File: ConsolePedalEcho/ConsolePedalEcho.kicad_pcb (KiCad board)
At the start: 2 copper layers, 100 x 60 mm, 56 parts, among them J1 Conn_02x25_Counter_Clockwise, U1 L78L05_TO92, U2 PT2399, U3 TL072

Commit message: Finished placing traces
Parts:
- moved C11 4.89 mm to (157.7, 103.9)
- moved C4 4.06 mm to (90.7, 82.0)
- moved C15 3.81 mm to (153.9, 103.9)
- moved C12 3.66 mm to (165.1, 105.2)
- moved C21 3.06 mm to (162.3, 100.3)
- moved D3 2.47 mm to (152.7, 95.0)
- moved R10 2.29 mm to (168.7, 107.7), turned to 90 degrees
- moved C9 2.08 mm to (138.4, 109.3)
- moved R17 1.52 mm to (124.0, 111.5)
- moved C6 1.40 mm to (127.3, 109.3)
- moved C7 1.27 mm to (135.4, 112.8)
- moved C8 1.27 mm to (135.4, 109.5)
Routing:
- net +9V: track 60.1 -> 181.3 mm, vias 2 -> 3
- net /LEDPower: track 54.1 -> 129.4 mm, vias 2 -> 4
- net Net-(R3-Pad1): track 0.00 -> 70.5 mm
- net Net-(C17-Pad2): track 0.00 -> 61.0 mm
- net Net-(C21-Pad1): track 0.00 -> 60.6 mm
- net Net-(D2-Pad1): track 0.54 -> 55.5 mm, vias 0 -> 1
- net Net-(C18-Pad2): track 0.00 -> 53.9 mm
- net Net-(C10-Pad1): track 0.00 -> 47.4 mm
- net Net-(C19-Pad2): track 0.00 -> 45.3 mm
- net Net-(C16-Pad2): track 0.00 -> 42.1 mm
- net Net-(C9-Pad2): track 0.00 -> 41.6 mm
- net Net-(C16-Pad1): track 0.00 -> 41.5 mm
- net Net-(C11-Pad2): track 0.00 -> 38.5 mm
- net /Output: track 65.8 -> 102.2 mm, vias 2 -> 3
- net Net-(C19-Pad1): track 0.00 -> 34.4 mm
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
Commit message: minor changes
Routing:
- net /Input: track 71.6 -> 100.6 mm
- net Net-(C12-Pad1): track 0.00 -> 26.3 mm
- net Net-(D2-Pad1): track 55.5 -> 71.4 mm
- net Net-(C11-Pad2): track 38.5 -> 53.2 mm
- net Net-(C11-Pad1): track 13.8 -> 26.0 mm
- net Net-(C21-Pad1): track 60.6 -> 65.6 mm
- net Net-(C15-Pad1): track 32.9 -> 35.5 mm
- added copper zone on F.Cu, net GND

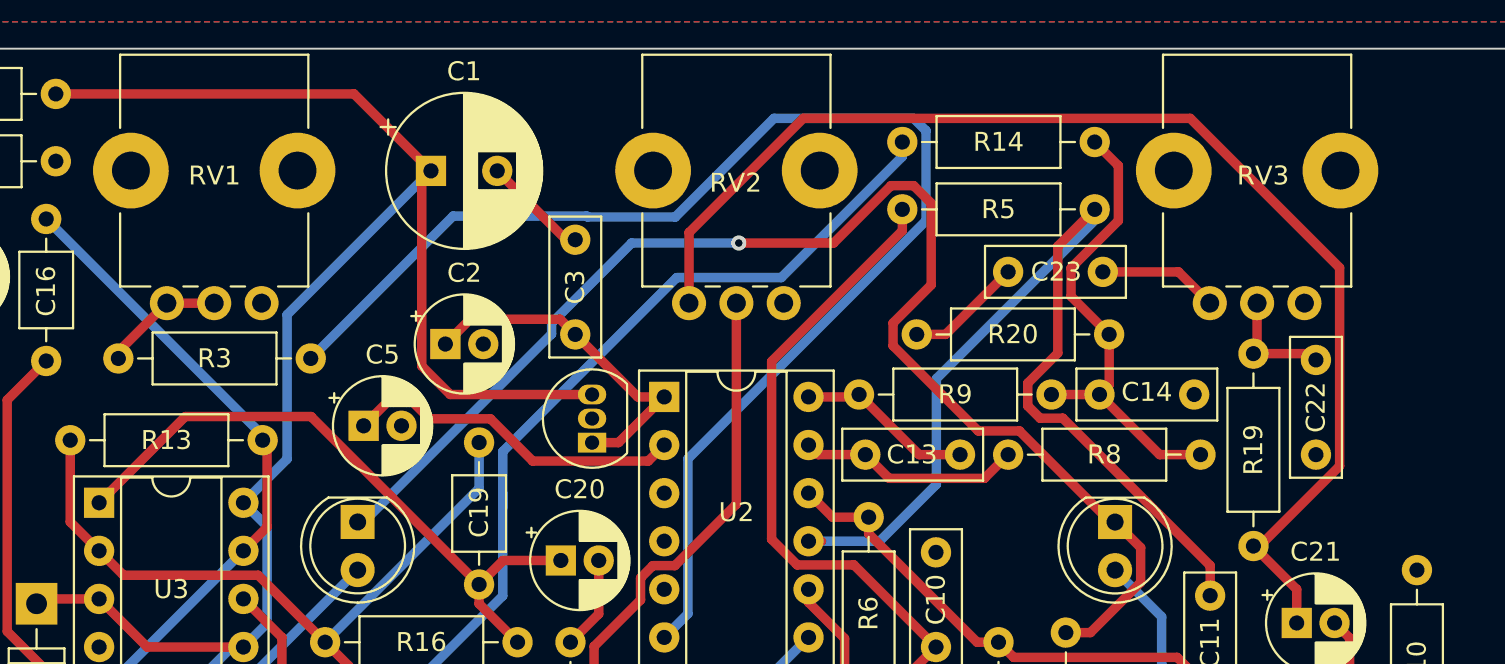
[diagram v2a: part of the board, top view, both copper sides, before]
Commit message: Flipped potentiometers around
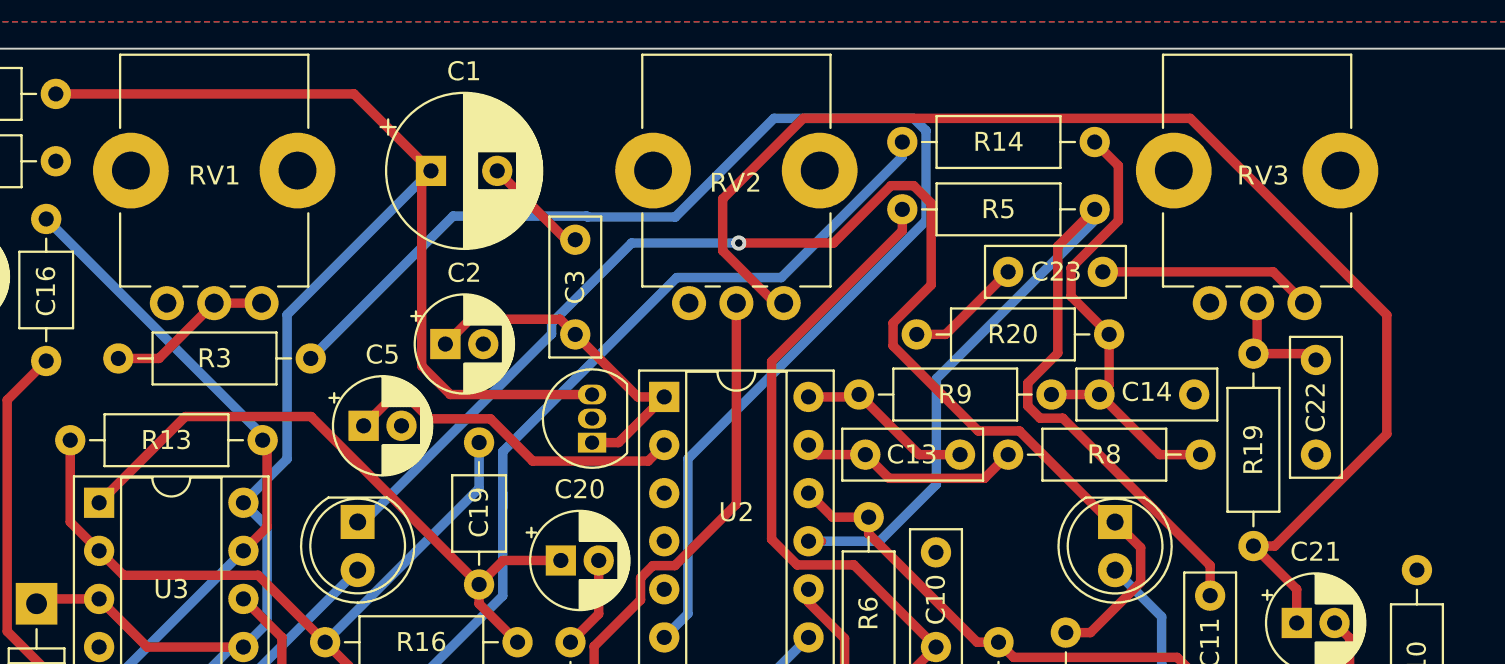
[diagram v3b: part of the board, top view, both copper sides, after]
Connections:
- RV1 pad 1: GND -> Net-(R3-Pad2)
- RV1 pad 3: Net-(R3-Pad2) -> GND
- RV2 pad 1: GND -> Net-(C21-Pad1)
- RV2 pad 3: Net-(C21-Pad1) -> GND
- RV3 pad 1: GND -> Net-(C23-Pad2)
- RV3 pad 3: Net-(C23-Pad2) -> GND
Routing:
- net Net-(C23-Pad2): track 6.33 -> 11.3 mm
- net Net-(C21-Pad1): track 65.6 -> 69.4 mm
- net Net-(R3-Pad2): track 6.48 -> 9.13 mm
